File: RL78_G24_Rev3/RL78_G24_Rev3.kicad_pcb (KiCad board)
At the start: 2 copper layers, 100 x 100 mm, 45 parts, among them P1 POWER_JACKPTH, P2 E2 Lite, P3 Keypad, P5 F09HP, P6 SPI_to_eth, P7 LCD-1.8, P8 SD_Connector, U1 R7F101GB, U2 AMS1117-3.3, U3 MCP23008-E_P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

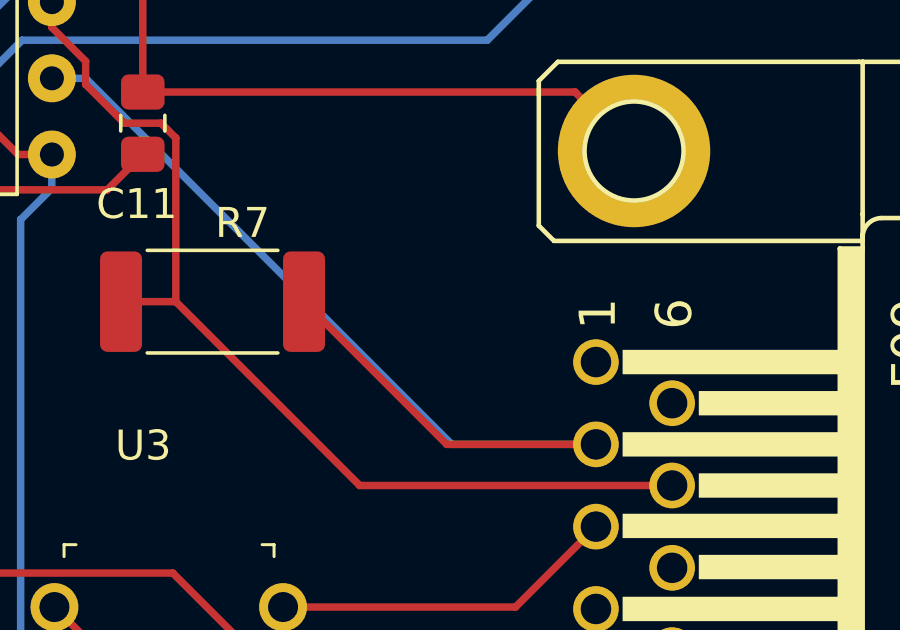
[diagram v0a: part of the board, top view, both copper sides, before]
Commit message: Added RL78/F14 project and added jumper for the 120 ohms resistors in the G24 project
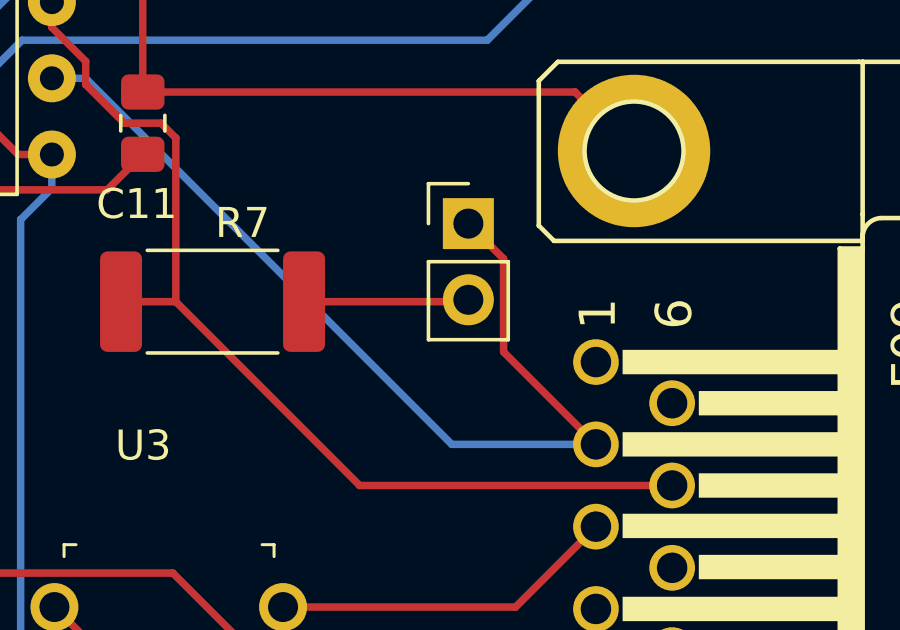
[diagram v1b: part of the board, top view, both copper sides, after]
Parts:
- added JP1: En term res, Connector_PinHeader_2.54mm:PinHeader_1x02_P2.54mm_Vertical, F.Cu at (155.2, 100.9)
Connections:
- P5 pad 2: Net-(U5-CANL) -> Net-(JP1-A)
- R7 pad 2: Net-(U5-CANL) -> Net-(JP1-B)
- U5 pad 6: Net-(U5-CANL) -> Net-(JP1-A)
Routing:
- net Net-(U5-CANL): track 34.9 -> 0.00 mm
- net Net-(JP1-A): track 0.00 -> 32.3 mm
- net Net-(JP1-B): track 0.00 -> 5.50 mm
